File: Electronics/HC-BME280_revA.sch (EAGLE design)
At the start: 18 parts, among them T2 AO3401, U1 ATMEGA328-20P, U2 NRF24L01, U3 BME280, U4 OLED128X64

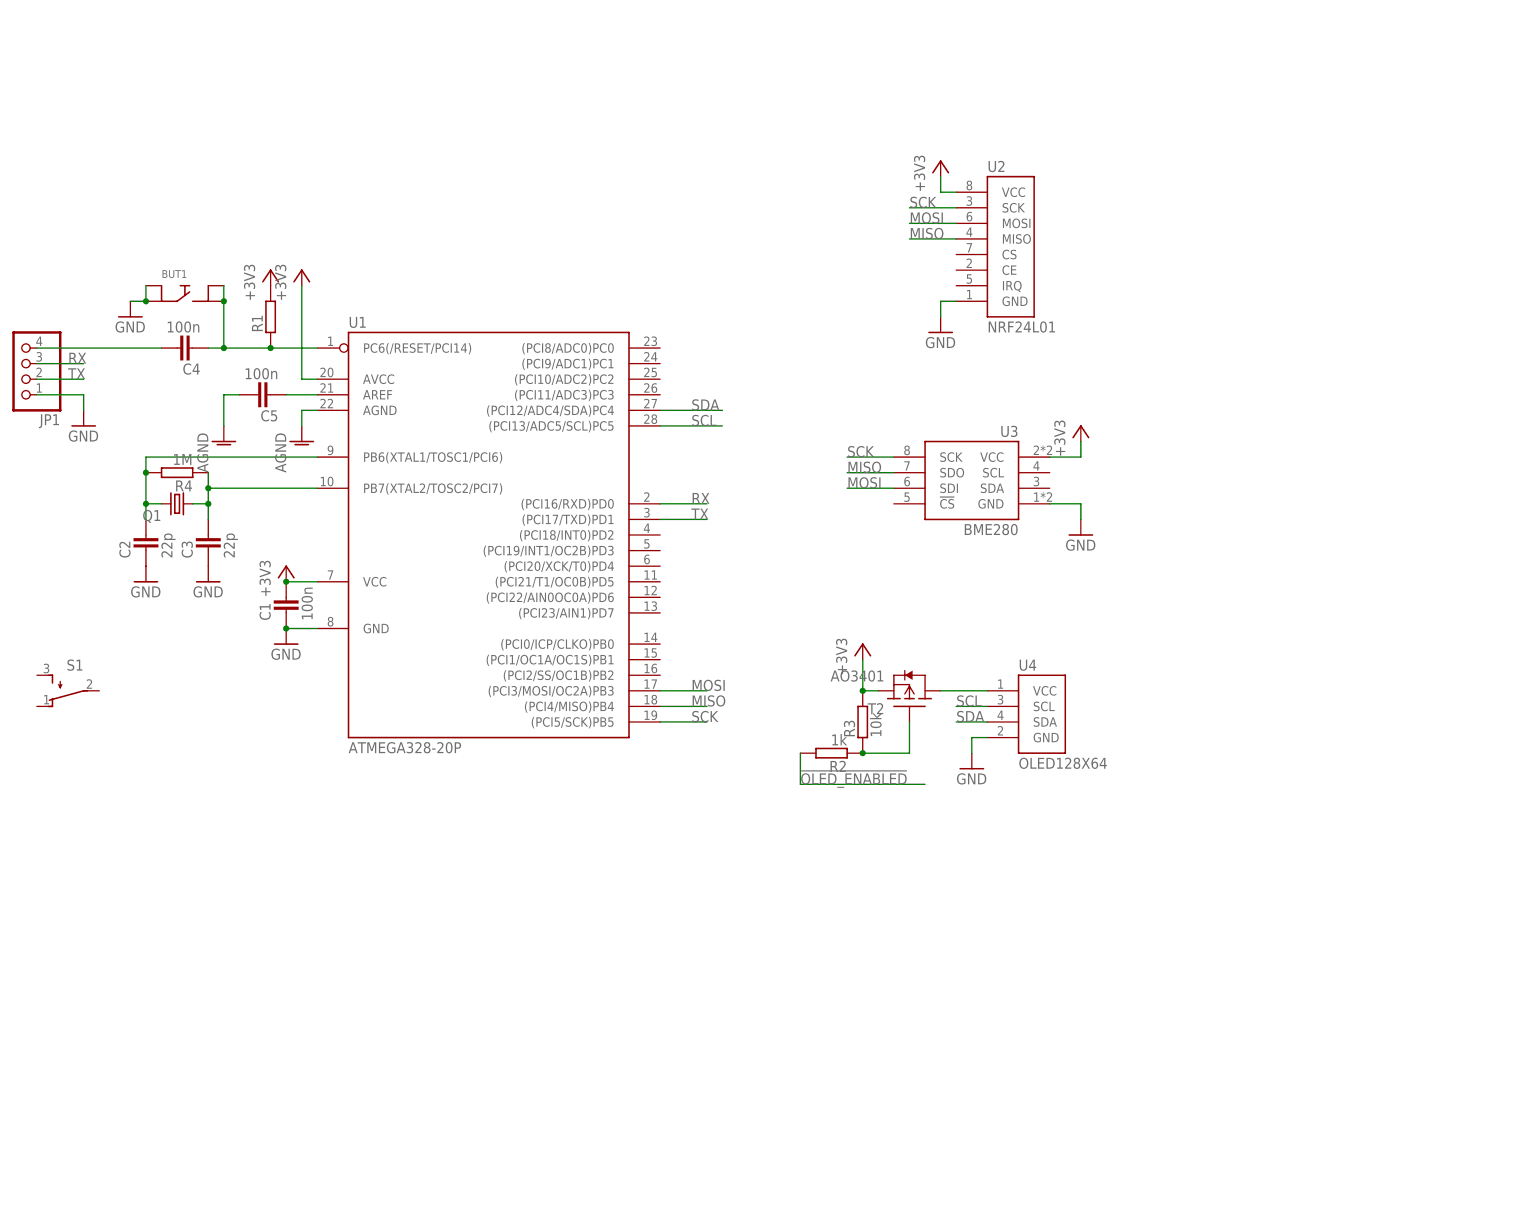
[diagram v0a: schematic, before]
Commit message: modified: diagram and PCB
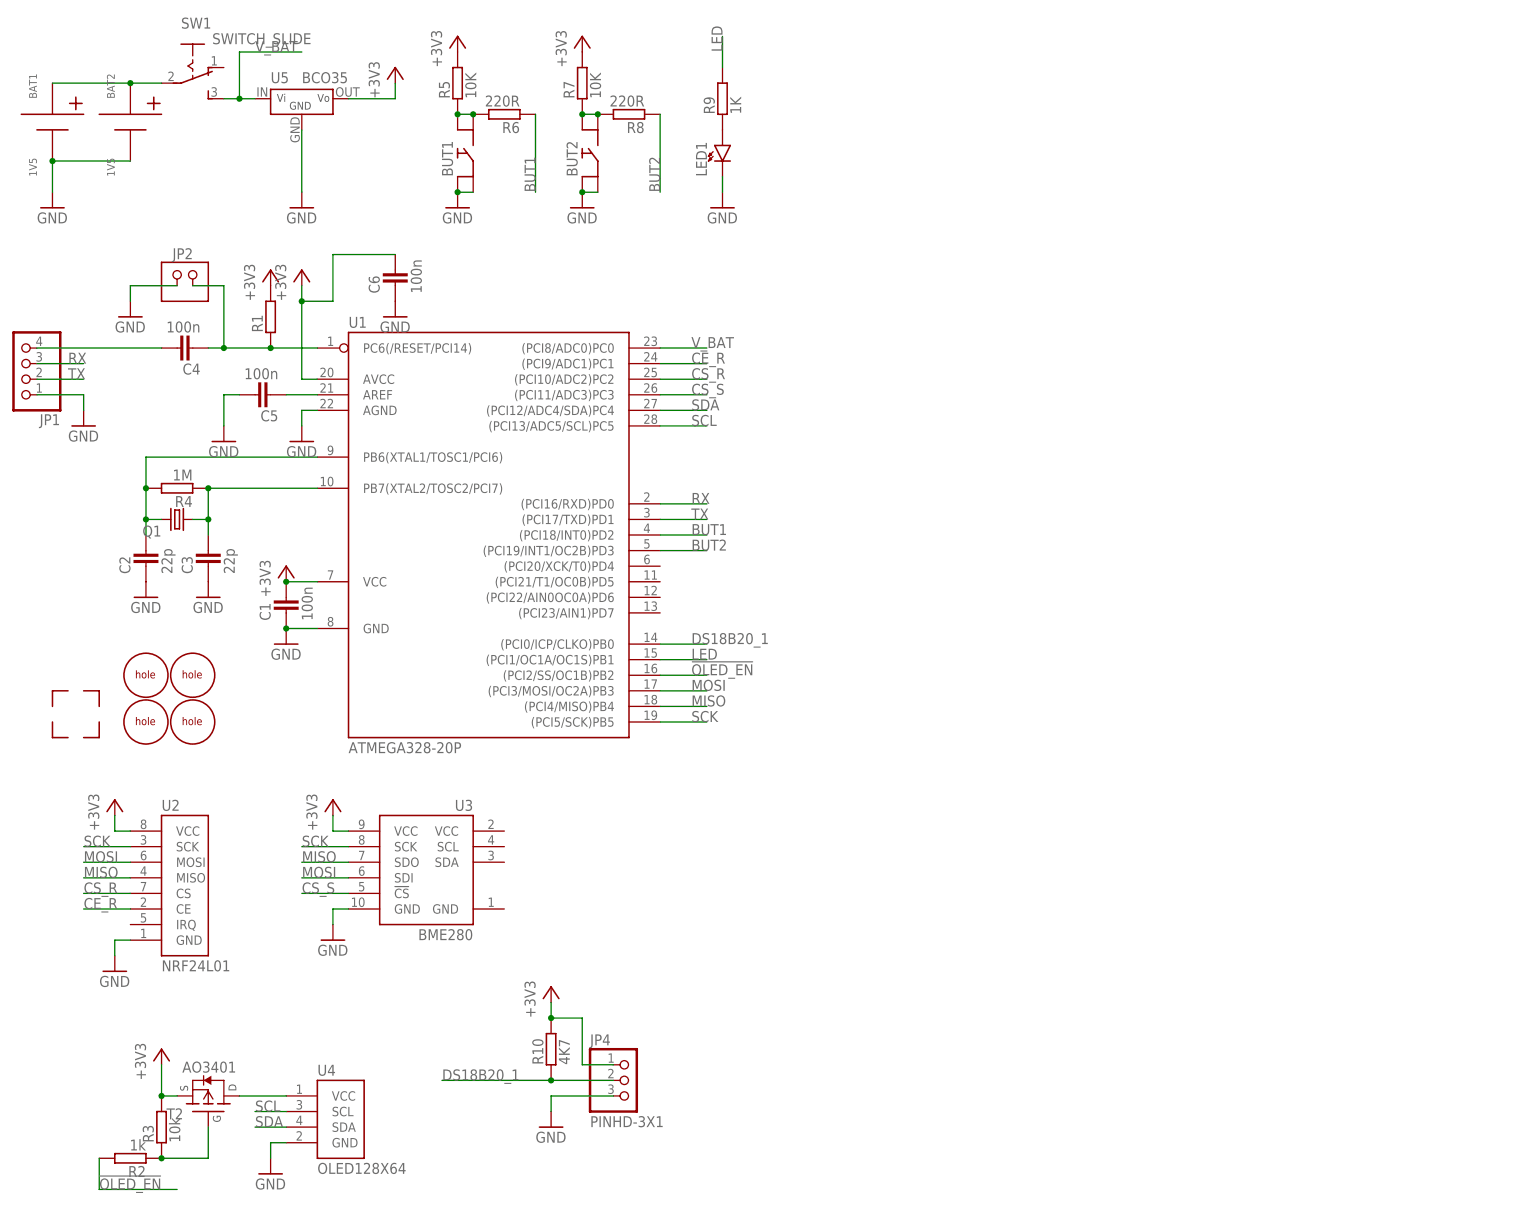
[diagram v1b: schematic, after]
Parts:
- removed S1: TL32WO'THT', 1_domaci:TL32WO'THT'
- added BAT1, BAT2: 1V5, 1_domaci:BATTERY_1X
- added BUT2: BUTTON'THT', 1_domaci:BUTTON'THT'
- added C6: 100n, 1_domaci:C-CERAMIC'SMD'
- added JP2: PINHD-2X1, 1_domaci:PINHD-2X1
- added JP4: PINHD-3X1, 1_domaci:PINHD-3X1
- added LED1: (no value), 1_domaci:LED'SMD'
- added R10: 4K7, 1_domaci:R'2'
- added R5, R7: 10K, 1_domaci:R'2'
- added R6, R8: 220R, 1_domaci:R'2'
- added R9: 1K, 1_domaci:R'2'
- added SW1: SWITCH_SLIDE, 1_domaci:SWITCH_SLIDE
- added U$1, U$2, U$3, U$4: CORNER, 1_domaci:CORNER
- added U$5, U$6, U$7, U$8: HOLE, 1_domaci:HOLE
- added U5: BCO35, 1_domaci:STEP_UP-BCO35
- JP1: device 1_domaci:PINHD-4X1'BASIC' -> 1_domaci:PINHD-4X1
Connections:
- removed net !OLED_ENABLED: R2.P$2
- removed net AGND: C5.P$2, U1.AGND
- new net !OLED_EN: R2.P$2, U1.(PCI2/SS/OC1B)PB2
- new net BUT1: R6.P$1, U1.(PCI18/INT0)PD2
- new net BUT2: R8.P$1, U1.(PCI19/INT1/OC2B)PD3
- new net CE_R: U1.(PCI9/ADC1)PC1, U2.CE
- new net CS_R: U1.(PCI10/ADC2)PC2, U2.CS
- new net CS_S: U1.(PCI11/ADC3)PC3, U3.!CS
- new net DS18B20_1: JP4.2, R10.P$1, U1.(PCI0/ICP/CLKO)PB0
- new net LED: R9.P$2, U1.(PCI1/OC1A/OC1S)PB1
- new net N$10: BUT2.1, BUT2.3, R7.P$1, R8.P$2
- new net N$11: LED1.A, R9.P$1
- new net N$8: BAT1.P, BAT2.P, SW1.MIDDLE
- new net N$9: BUT1.1, BUT1.3, R5.P$1, R6.P$2
- new net V_BAT: SW1.S, U1.(PCI8/ADC0)PC0, U5.VIN
- net +3V3: now also C6.P$2, JP4.1, R10.P$2, R5.P$2, R7.P$2, U3.VCC@SPI, U5.VOUT; no longer U3.VCC
- net GND: now also BAT1.N, BAT2.N, BUT2.2, BUT2.4, C5.P$2, C6.P$1, JP2.1, JP4.3, LED1.K, U1.AGND, U3.GND@SPI, U5.GND; no longer U3.GND
- net N$2: now also JP2.2; no longer BUT1.1, BUT1.3
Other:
- moved on the sheet: BUT1, C2, C3, Q1, R2, R3, R4, U2, U4

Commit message: modified: PCB - revA
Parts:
- removed JP1: (no value), 1_domaci:PINHD-4X1
- added JP3: (no value), 1_domaci:PINHD-4X1
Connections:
- net GND: now also JP3.4; no longer JP1.1
- net N$6: now also JP3.1; no longer JP1.4
- net RX: now also JP3.2; no longer JP1.3
- net TX: now also JP3.3; no longer JP1.2
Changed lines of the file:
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@@
 <part name="GND3" library="supply1" deviceset="GND" device=""/>
 <part name="GND4" library="supply1" deviceset="GND" device=""/>
-<part name="JP1" library="1_domaci" deviceset="PINHD-4X1" device=""/>
 <part name="GND5" library="supply1" deviceset="GND" device=""/>
 <part name="GND6" library="supply1" deviceset="GND" device=""/>
@@
 <part name="+3V11" library="supply1" deviceset="+3V3" device=""/>
 <part name="GND18" library="supply1" deviceset="GND" device=""/>
+<part name="JP3" library="1_domaci" deviceset="PINHD-4X1" device=""/>
 </parts>
 <sheets>
@@
 <instance part="GND3" gate="1" x="-15.24" y="43.18"/>
 <instance part="GND4" gate="1" x="-27.94" y="88.9"/>
-<instance part="JP1" gate="A" x="-45.72" y="81.28" rot="R180"/>
 <instance part="GND5" gate="1" x="-35.56" y="71.12"/>
 <instance part="GND6" gate="1" x="-5.08" y="-50.8"/>
@@
 <instance part="+3V11" gate="G$1" x="5.08" y="10.16"/>
 <instance part="GND18" gate="1" x="5.08" y="-12.7"/>
+<instance part="JP3" gate="A" x="-45.72" y="78.74" rot="MR0"/>
 </instances>
 <busses>
@@
 <wire x1="-43.18" y1="78.74" x2="-35.56" y2="78.74" width="0.1524" layer="91"/>
 <label x="-38.1" y="78.74" size="1.778" layer="95"/>
-<pinref part="JP1" gate="A" pin="2"/>
+<pinref part="JP3" gate="A" pin="3"/>
 </segment>
 </net>
@@
 <wire x1="-43.18" y1="81.28" x2="-35.56" y2="81.28" width="0.1524" layer="91"/>
 <label x="-38.1" y="81.28" size="1.778" layer="95"/>
-<pinref part="JP1" gate="A" pin="3"/>
+<pinref part="JP3" gate="A" pin="2"/>
 </segment>
 </net>
@@
 <pinref part="C4" gate="G$1" pin="P$2"/>
 <wire x1="-22.86" y1="83.82" x2="-43.18" y2="83.82" width="0.1524" layer="91"/>
-<pinref part="JP1" gate="A" pin="4"/>
+<pinref part="JP3" gate="A" pin="1"/>
 </segment>
 </net>
@@
 </segment>
 <segment>
-<pinref part="JP1" gate="A" pin="1"/>
 <pinref part="GND5" gate="1" pin="GND"/>
 <wire x1="-43.18" y1="76.2" x2="-35.56" y2="76.2" width="0.1524" layer="91"/>
 <wire x1="-35.56" y1="76.2" x2="-35.56" y2="73.66" width="0.1524" layer="91"/>
-</segment>
-<segment>
+<pinref part="JP3" gate="A" pin="4"/>
+</segment>
+<segment>

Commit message: modified: minor changes in schematics and PCB
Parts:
- JP2: value PINHD-2X1 -> PINHD2X1
- JP3: value (none) -> PINHD3X1
- LED1: value (none) -> green
- Q1: value (none) -> 16MHz
- R1: value (none) -> 4k7
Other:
- note added: "1. pull up pred mosfetem je 47k 2. RF modul nema pripojene napajeni"
- note added: "HC-BME280 Rev.A"
- moved on the sheet: BAT1, BAT2, BUT1, BUT2, C1, C2, C3, C4, C5, C6, JP2, JP3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

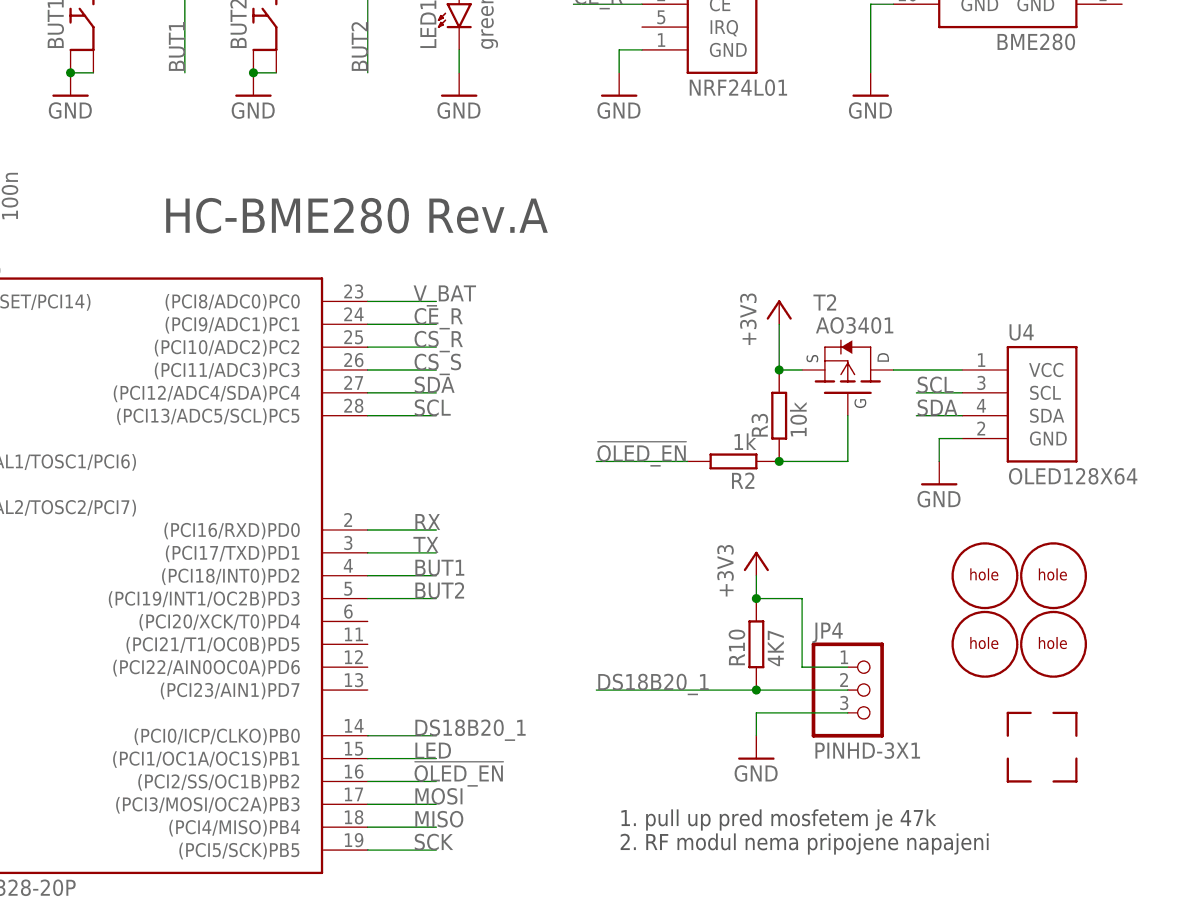
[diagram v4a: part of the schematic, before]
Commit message: added: comments to schematic
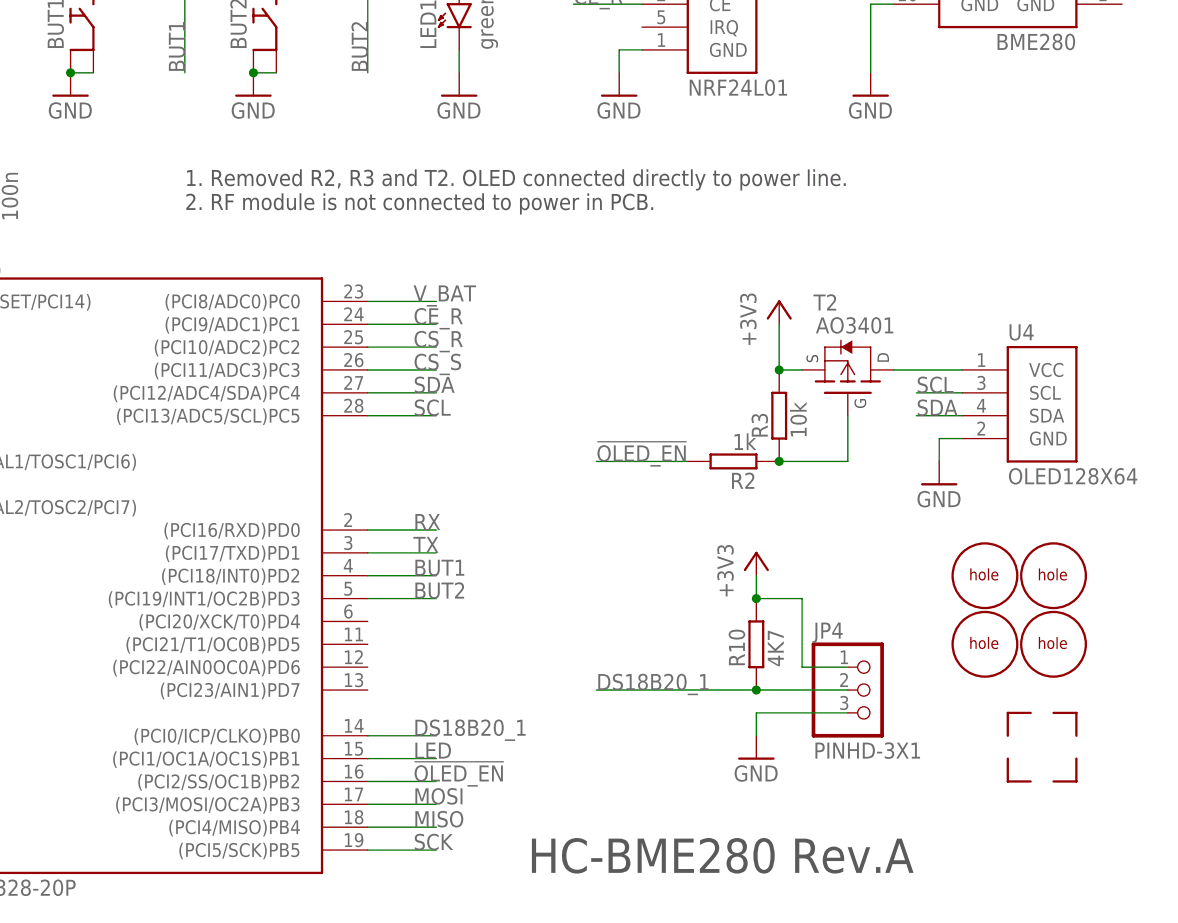
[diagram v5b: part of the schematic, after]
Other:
- note added: "1. Removed R2, R3 and T2. OLED connected directly to power line. 2. RF module is not connected to power in PCB."
- note removed: "1. pull up pred mosfetem je 47k 2. RF modul nema pripojene napajeni"
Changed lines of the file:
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@@
 <sheet>
 <plain>
-<text x="139.7" y="7.62" size="1.778" layer="97">1. pull up pred mosfetem je 47k
-2. RF modul nema pripojene napajeni</text>
-<text x="88.9" y="76.2" size="3.81" layer="97">HC-BME280 Rev.A</text>
+<text x="91.44" y="78.74" size="1.778" layer="97">1. Removed R2, R3 and T2. OLED connected directly to power line.
+2. RF module is not connected to power in PCB.</text>
+<text x="129.54" y="5.08" size="3.81" layer="97">HC-BME280 Rev.A</text>
 </plain>
 <instances>
